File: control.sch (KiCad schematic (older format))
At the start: 24 parts, among them J301 ROT_OUT, J302 DEBUG, J303 ROT_IN, J304 DISPLAY, SW301 Encoder, U301 STM32F030F4Px, U302 24LC1025, Y301 MA-506-8MHz

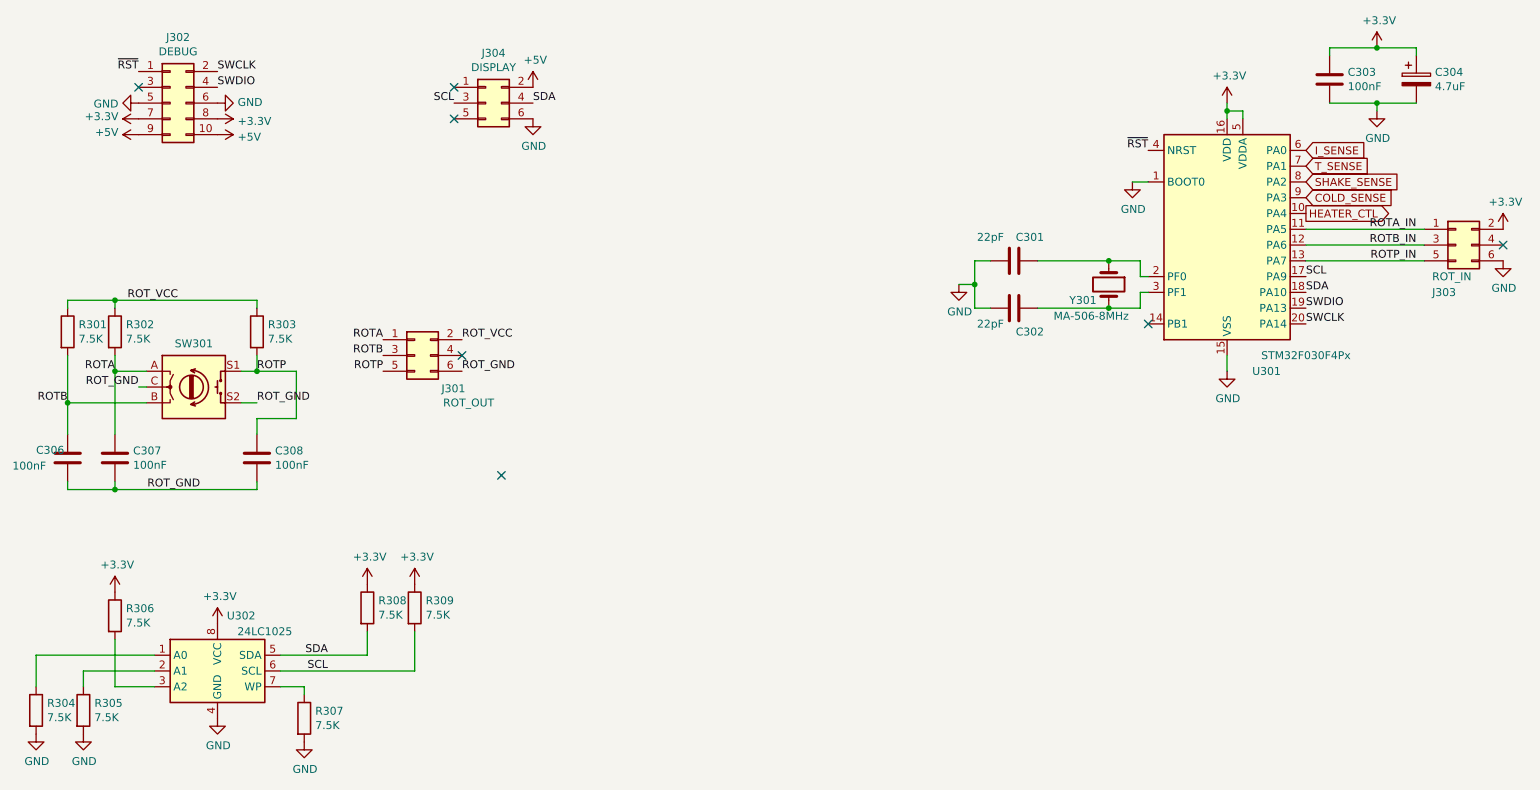
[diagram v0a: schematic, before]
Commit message: Fix ST12 schematics with current sensor (tested on balcony patch)
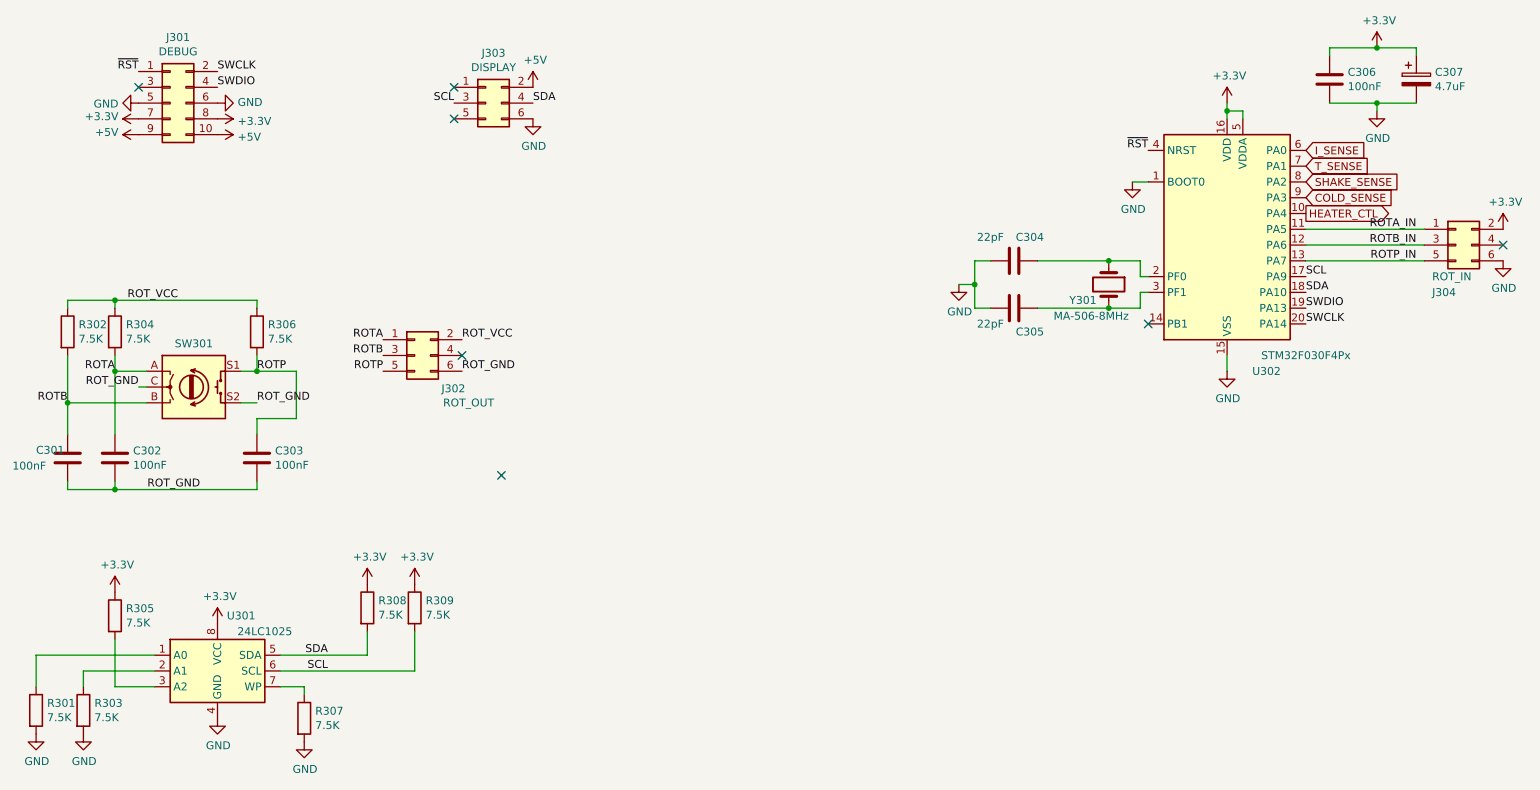
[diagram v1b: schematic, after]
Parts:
- renumbered C306 to C301, C307 to C302, C308 to C303, C301 to C304, C302 to C305, C303 to C306, C304 to C307, J302 to J301, J301 to J302, J304 to J303, J303 to J304, R304 to R301, R301 to R302, R305 to R303, R302 to R304, R306 to R305, R303 to R306, U302 to U301, U301 to U302
